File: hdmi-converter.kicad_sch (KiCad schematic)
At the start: 126 parts, among them J2 46756-1001, Q1 BSS138APW, Q2 BSS138APW, Q3 BSS138APW, Q4 BSS138APW, U2 TXB0104RUT, U3 LT9611, Y2 ABM8G-24.000MHZ-18-D2Y-T

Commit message: Introduce component standardization
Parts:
- C18, C20, C27, C28, C29, C30, C31, C32, C33, C35, C37, C39, C40, C41, C42, C45, C46, C47, C48, C49, C50, C51, C52, C53, C55: footprint sa800u-baseboard-hw-footprints:0402-cap -> sa800u-baseboard-hw-footprints:C_0402_1005Metric; Author (none) -> Antmicro; Dielectric (none) -> X5R; License (none) -> Apache-2.0; MPN 0402X104K6R3CT -> GRM155R61H104KE14D; Manufacturer Walsin -> Murata; Voltage (none) -> 50V
- C19, C21: footprint sa800u-baseboard-hw-footprints:0402-cap -> sa800u-baseboard-hw-footprints:C_0402_1005Metric; Author (none) -> Antmicro; License (none) -> Apache-2.0; Manufacturer MULTICOMP -> Multicomp
- C22, C23, C24, C36, C38, C43: footprint sa800u-baseboard-hw-footprints:0402-cap -> sa800u-baseboard-hw-footprints:C_0402_1005Metric; Author (none) -> Antmicro; License (none) -> Apache-2.0; MPN GRM155R60J106ME44D -> CC0402MRX5R5BB106; Manufacturer MURATA -> Yaego
- C25, C26, C34: footprint sa800u-baseboard-hw-footprints:0402-cap -> sa800u-baseboard-hw-footprints:C_0402_1005Metric; Author (none) -> Antmicro; License (none) -> Apache-2.0
- C44, C54: renamed from C?; value (none) -> C_100n_0402; footprint (none) -> sa800u-baseboard-hw-footprints:C_0402_1005Metric; Author (none) -> Antmicro; Dielectric (none) -> X5R; License (none) -> Apache-2.0; Voltage (none) -> 50V
- C56, C57: footprint sa800u-baseboard-hw-footprints:0402-cap -> sa800u-baseboard-hw-footprints:C_0402_1005Metric; Author (none) -> Antmicro; Dielectric (none) -> C0G; License (none) -> Apache-2.0; MPN MC0402N100D500CT -> GCM1555C1H100GA16D; Manufacturer MULTICOMP -> Murata; Voltage (none) -> 50V
- D1: renamed from D?; value (none) -> 1N4148WS; footprint (none) -> sa800u-baseboard-hw-footprints:D_SOD-323F; Author (none) -> Antmicro; License (none) -> Apache-2.0
- D2: footprint sa800u-baseboard-hw-footprints:SOD-323F -> sa800u-baseboard-hw-footprints:D_SOD-323F; Author (none) -> Antmicro; License (none) -> Apache-2.0
- D3, D4, D5: footprint sa800u-baseboard-hw-footprints:PUSB3F96X -> sa800u-baseboard-hw-footprints:Nexperia_DFN-10_2.5x1mm_P0.5mm; Author (none) -> Antmicro; License (none) -> Apache-2.0
- FB2: value BLM18SG121TN1D -> FB_120Z_3A_0603; footprint sa800u-baseboard-hw-footprints:0603-res -> sa800u-baseboard-hw-footprints:FB_0603_1608Metric; symbol sa800u-baseboard-hw:BLM18SG121TN1D -> sa800u-baseboard-hw:FB_120Z_3A_0603; Author (none) -> Antmicro; License (none) -> Apache-2.0; Manufacturer Murata Electronics North America -> Murata
- J2: value 46756-1001 -> HDMI_Micro-D_46756-1001; symbol sa800u-baseboard-hw:46756-1001 -> sa800u-baseboard-hw:HDMI_Micro-D_46756-1001; Author (none) -> Antmicro; License (none) -> Apache-2.0
- L1, L2, L3, L4, L5, L6: value BRC1608TR35M -> L_350n_1.4A_0603; footprint sa800u-baseboard-hw-footprints:INDC1608X100N -> sa800u-baseboard-hw-footprints:L_0603_1608Metric; symbol sa800u-baseboard-hw:BRC1608TR35M -> sa800u-baseboard-hw:L_350n_1.4A_0603; Author (none) -> Antmicro; License (none) -> Apache-2.0; Val (none) -> 350n/1.4A
- L10, L7, L8, L9: footprint sa800u-baseboard-hw-footprints:FIL_NFP0QHB242HS2D -> sa800u-baseboard-hw-footprints:L_Murata_025020_0605Metric; Author (none) -> Antmicro; License (none) -> Apache-2.0; Manufacturer MURATA -> Murata
- Q1, Q2, Q3, Q4: value BSS138APW -> BSS138PW; symbol sa800u-baseboard-hw:BSS138APW -> sa800u-baseboard-hw:BSS138PW; Author (none) -> Antmicro; License (none) -> Apache-2.0; Manufacturer ON Semiconductor -> Nexperia
- R15: footprint sa800u-baseboard-hw-footprints:0402-res -> sa800u-baseboard-hw-footprints:R_0402_1005Metric; Author (none) -> Antmicro; License (none) -> Apache-2.0; Manufacturer BOURNS -> Bourns; Tolerance (none) -> 1%
- R16, R30, R31: footprint sa800u-baseboard-hw-footprints:0402-res -> sa800u-baseboard-hw-footprints:R_0402_1005Metric; Author (none) -> Antmicro; Current (none) -> 1A; License (none) -> Apache-2.0; Manufacturer PANASONIC -> Panasonic
- R17, R29, R41, R50: footprint sa800u-baseboard-hw-footprints:0402-res -> sa800u-baseboard-hw-footprints:R_0402_1005Metric; Author (none) -> Antmicro; License (none) -> Apache-2.0; MPN CRCW040210K0FKEDHP -> CR0402-FX-1002GLF; Manufacturer VISHAY -> Bourns; Tolerance (none) -> 1%
- R18, R19, R20, R23, R24, R25, R26: footprint sa800u-baseboard-hw-footprints:0402-res -> sa800u-baseboard-hw-footprints:R_0402_1005Metric; Author (none) -> Antmicro; License (none) -> Apache-2.0; MPN MCS04020C4701FE000 -> CR0402-FX-4701GLF; Manufacturer VISHAY -> Bourns; Tolerance (none) -> 1%
- R21: renamed from R?; value (none) -> R_1M_0402; footprint (none) -> sa800u-baseboard-hw-footprints:R_0402_1005Metric; symbol sa800u-baseboard-hw:R_1M0_0402 -> sa800u-baseboard-hw:R_1M_0402; Author (none) -> Antmicro; License (none) -> Apache-2.0; MPN CRG0402F1M0 -> CR0402-FX-1004GLF; Manufacturer TE CONNECTIVITY -> Bourns; Tolerance (none) -> 1%; Val 1M0 -> 1M
- R22: footprint sa800u-baseboard-hw-footprints:0402-res -> sa800u-baseboard-hw-footprints:R_0402_1005Metric; Author (none) -> Antmicro; License (none) -> Apache-2.0; MPN RC0402FR-077K68L -> CR0402-FX-7681GLF; Manufacturer Yageo -> Bourns; Tolerance (none) -> 1%
- R27, R43: footprint sa800u-baseboard-hw-footprints:0402-res -> sa800u-baseboard-hw-footprints:R_0402_1005Metric; Author (none) -> Antmicro; License (none) -> Apache-2.0; MPN CRCW040220K0FKED -> CR0402-FX-2002GLF; Manufacturer VISHAY -> Bourns; Tolerance (none) -> 1%
- R28, R32: footprint sa800u-baseboard-hw-footprints:0402-res -> sa800u-baseboard-hw-footprints:R_0402_1005Metric; Author (none) -> Antmicro; License (none) -> Apache-2.0; MPN RC0402FR-072K2L -> CR0402-FX-2201GLF; Manufacturer YAGEO -> Bourns; Tolerance (none) -> 1%
- R33: footprint sa800u-baseboard-hw-footprints:0402-res -> sa800u-baseboard-hw-footprints:R_0402_1005Metric; Author (none) -> Antmicro; License (none) -> Apache-2.0; MPN ERJ2RKF2702X -> CR0402-FX-2702GLF; Manufacturer PANASONIC_ELECTRONIC_COMPONENTS -> Bourns; Tolerance (none) -> 1%
- R34, R36, R44, R46: renamed from R?; value (none) -> R_2k_0402; footprint (none) -> sa800u-baseboard-hw-footprints:R_0402_1005Metric; Author (none) -> Antmicro; License (none) -> Apache-2.0; MPN CRCW04022K00FKED -> CR0402-FX-2001GLF; Manufacturer VISHAY -> Bourns; Tolerance (none) -> 1%
- R35, R37, R38, R39, R40, R42, R45, R47: footprint sa800u-baseboard-hw-footprints:0402-res -> sa800u-baseboard-hw-footprints:R_0402_1005Metric; Author (none) -> Antmicro; License (none) -> Apache-2.0; MPN RN73R1ETTP50R0F50 -> CR0402-FX-50R0GLF; Manufacturer KOA -> Bourns; Tolerance (none) -> 1%
- R48, R49, R51, R52, R53, R54, R55, R56: footprint sa800u-baseboard-hw-footprints:0402-res -> sa800u-baseboard-hw-footprints:R_0402_1005Metric; Author (none) -> Antmicro; License (none) -> Apache-2.0; MPN RC0402JR-07510RL -> CR0402-FX-5100GLF; Manufacturer Yageo -> Bourns; Tolerance (none) -> 1%
- TP10, TP11, TP12, TP13, TP14, TP15, TP16, TP19: value TP_SMD_0_75MM -> TP_0.75mm_SMD; footprint sa800u-baseboard-hw-footprints:Testpoint_smd_0_75mm -> sa800u-baseboard-hw-footprints:TP_SMD_0.75mm; symbol sa800u-baseboard-hw:TP_SMD_0_75MM -> sa800u-baseboard-hw:TP_0.75mm_SMD; Author (none) -> Antmicro; License (none) -> Apache-2.0
- TP17, TP18, TP20, TP21, TP22, TP23, TP24, TP25, TP26, TP9: renamed from TP?; value (none) -> TP_0.75mm_SMD; footprint (none) -> sa800u-baseboard-hw-footprints:TP_SMD_0.75mm; symbol sa800u-baseboard-hw:TP_SMD_0_75MM -> sa800u-baseboard-hw:TP_0.75mm_SMD; Author (none) -> Antmicro; License (none) -> Apache-2.0
- TP27: renamed from TP?; value (none) -> TP_0.75mm_SMD; footprint (none) -> sa800u-baseboard-hw-footprints:TP_SMD_0.75mm; symbol sa800u-baseboard-hw:TP -> sa800u-baseboard-hw:TP_0.75mm_SMD; Author (none) -> Antmicro; License (none) -> Apache-2.0
- U2: value TXB0104RUT -> TXB0104_UQFN; footprint sa800u-baseboard-hw-footprints:Texas_R_PUQFN-N12 -> sa800u-baseboard-hw-footprints:UQFN-12_2x1.7mm_P0.4mm_Texas_RUT; symbol sa800u-baseboard-hw:TXB0104RUT -> sa800u-baseboard-hw:TXB0104_UQFN; Author (none) -> Antmicro; License (none) -> Apache-2.0
- U3: footprint sa800u-baseboard-hw-footprints:LT9611 -> sa800u-baseboard-hw-footprints:QFN-64-1EP_7.5x7.5mm_P0.4mm; Author (none) -> Antmicro; License (none) -> Apache-2.0; Manufacturer LONTIUM -> Lontium
- U4: renamed from U?; value (none) -> NTS0102_XSON; footprint (none) -> sa800u-baseboard-hw-footprints:XSON-8_1x1.95mm_P0.5mm; symbol sa800u-baseboard-hw:NTS0102GT -> sa800u-baseboard-hw:NTS0102_XSON; Author (none) -> Antmicro; License (none) -> Apache-2.0; Manufacturer NXP Semiconductors -> NXP
- Y2: footprint sa800u-baseboard-hw-footprints:KX-7 -> sa800u-baseboard-hw-footprints:Oscillator_SMD_Geyer_KX-7-4Pin_3.2x2.5mm; Author (none) -> Antmicro; License (none) -> Apache-2.0; Manufacturer ABRACON -> Abracon; Val (none) -> 24.000MHz
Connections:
- net GND: now also C18.2; no longer C18.1
- net HDMI_CLK_N: now also C49.2; no longer C49.1
- net HDMI_CLK_P: now also C53.2; no longer C53.1
- net HDMI_TX0_N: now also C48.2; no longer C48.1
- net HDMI_TX0_P: now also C52.2; no longer C52.1
- net HDMI_TX1_N: now also C47.2; no longer C47.1
- net HDMI_TX1_P: now also C51.2; no longer C51.1
- net HDMI_TX2_N: now also C46.2; no longer C46.1
- net HDMI_TX2_P: now also C50.2; no longer C50.1
- net HDMI_TX_CLK_N: now also C49.1; no longer C49.2
- net HDMI_TX_CLK_P: now also C53.1; no longer C53.2
- net HDMI_TX_D0_N: now also C48.1; no longer C48.2
- net HDMI_TX_D0_P: now also C52.1; no longer C52.2
- net HDMI_TX_D1_N: now also C47.1; no longer C47.2
- net HDMI_TX_D1_P: now also C51.1; no longer C51.2
- net HDMI_TX_D2_N: now also C46.1; no longer C46.2
- net HDMI_TX_D2_P: now also C50.1; no longer C50.2
- net VREG_S4A_1V8: now also C18.1; no longer C18.2
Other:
- moved on the sheet: C18, C19, C20, C21, C22, C23, C24, C25, C26, C27, C28, C29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

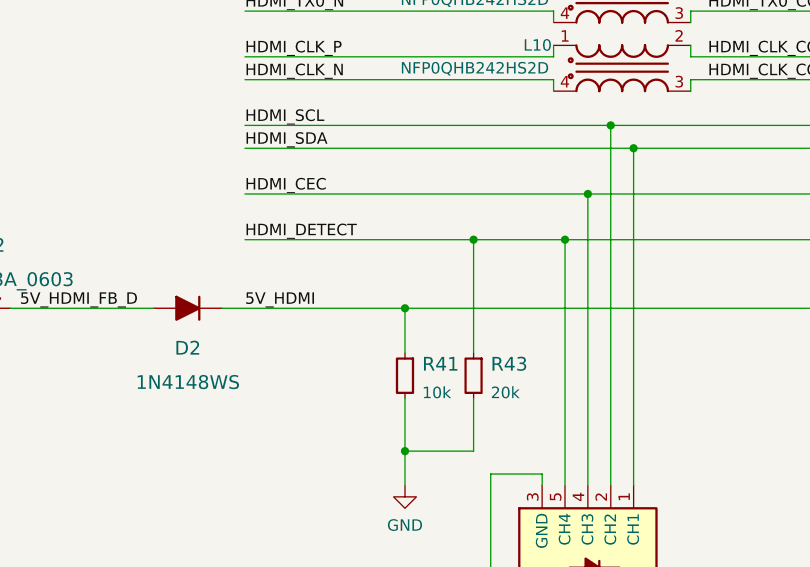
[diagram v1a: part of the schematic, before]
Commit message: Add OHP assets
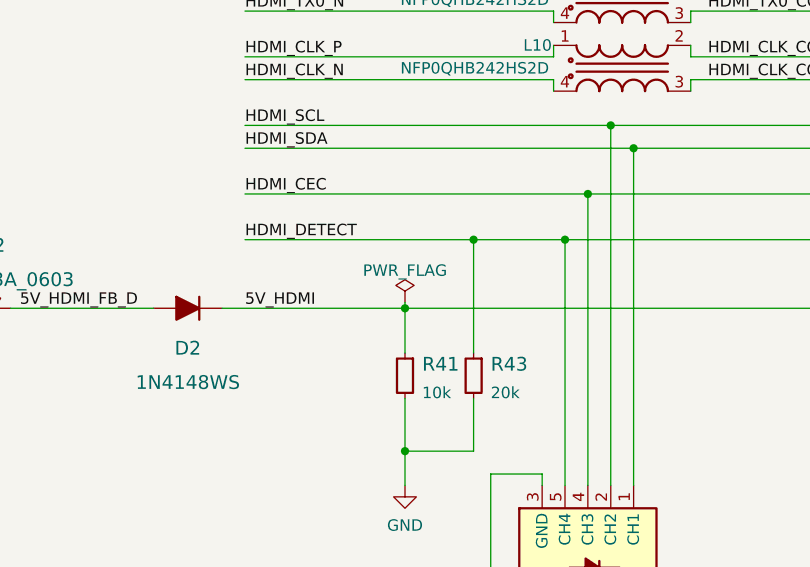
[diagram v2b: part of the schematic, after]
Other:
- company: (none) -> Antmicro Ltd.
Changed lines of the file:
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@@
   (title_block
     (title "SA800U (Snapdragon 845) Baseboard")
-    (date "2023-07-27")
-    (rev "1.0.2")
+    (date "2023-10-19")
+    (rev "1.0.3")
+    (company "Antmicro Ltd.")
     (comment 1 "www.antmicro.com")
-    (comment 2 "Antmicro Ltd.")
   )
   (junction (at 69.85 177.165) (diameter 0) (color 0 0 0 0)
@@
     (stroke (width 0) (type default) (color 0 0 0 0))
   )
+  (wire (pts (xy 272.415 73.66) (xy 272.415 74.295))
+    (stroke (width 0) (type default) (color 0 0 0 0))
+  )
   (wire (pts (xy 58.42 111.125) (xy 58.42 109.855))
     (stroke (width 0) (type default) (color 0 0 0 0))
@@
     (pin "1")
   )
-  (symbol (lib_id "sa800u-baseboard-hw:NFP0QHB242HS2D") (at 288.925 22.225 0) (unit 1)
+  (symbol (lib_name "NFP0QHB242HS2D_2") (lib_id "sa800u-baseboard-hw:NFP0QHB242HS2D") (at 288.925 22.225 0) (unit 1)
     (in_bom yes) (on_board yes)
     (property "Reference" "L7" (id 0) (at 287.147 22.225 0))
@@
     (pin "1")
   )
-  (symbol (lib_id "sa800u-baseboard-hw:NFP0QHB242HS2D") (at 288.925 29.845 0) (unit 1)
+  (symbol (lib_name "NFP0QHB242HS2D_3") (lib_id "sa800u-baseboard-hw:NFP0QHB242HS2D") (at 288.925 29.845 0) (unit 1)
     (in_bom yes) (on_board yes)
     (property "Reference" "L8" (id 0) (at 287.147 29.845 0))
@@
     (pin "4")
   )
-  (symbol (lib_id "sa800u-baseboard-hw:NFP0QHB242HS2D") (at 288.925 37.465 0) (unit 1)
+  (symbol (lib_name "NFP0QHB242HS2D_1") (lib_id "sa800u-baseboard-hw:NFP0QHB242HS2D") (at 288.925 37.465 0) (unit 1)
     (in_bom yes) (on_board yes)
     (property "Reference" "L9" (id 0) (at 287.147 37.465 0))
@@
     )
     (pin "1")
+  )
+  (symbol (lib_id "sa800u-baseboard-hw:PWR_FLAG") (at 272.415 73.66 0) (unit 1)
+    (in_bom yes) (on_board yes)
+    (property "Reference" "#FLG0105" (id 0) (at 272.415 71.755 0)
+      (effects (font (size 1.27 1.27)) hide)
+    )
+    (property "Value" "PWR_FLAG" (id 1) (at 272.415 70.104 0))
+    (property "Footprint" "" (id 2) (at 272.415 73.66 0)
+      (effects (font (size 1.27 1.27)) hide)
+    )
+    (property "Datasheet" "~" (id 3) (at 272.415 73.66 0)
+      (effects (font (size 1.27 1.27)) hide)
+    )
+    (pin "1")
